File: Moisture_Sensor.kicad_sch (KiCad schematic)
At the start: 17 parts, among them J1 UPDI, J2 OLED SSD1306 0.96in, J3 STEMMA QT soil sensor, J5 BATTERY 2xAAA, Q1 DMG3415U, SW1 READ, U1 ATtiny1614-SSNR, U2 TPS22917DBVR

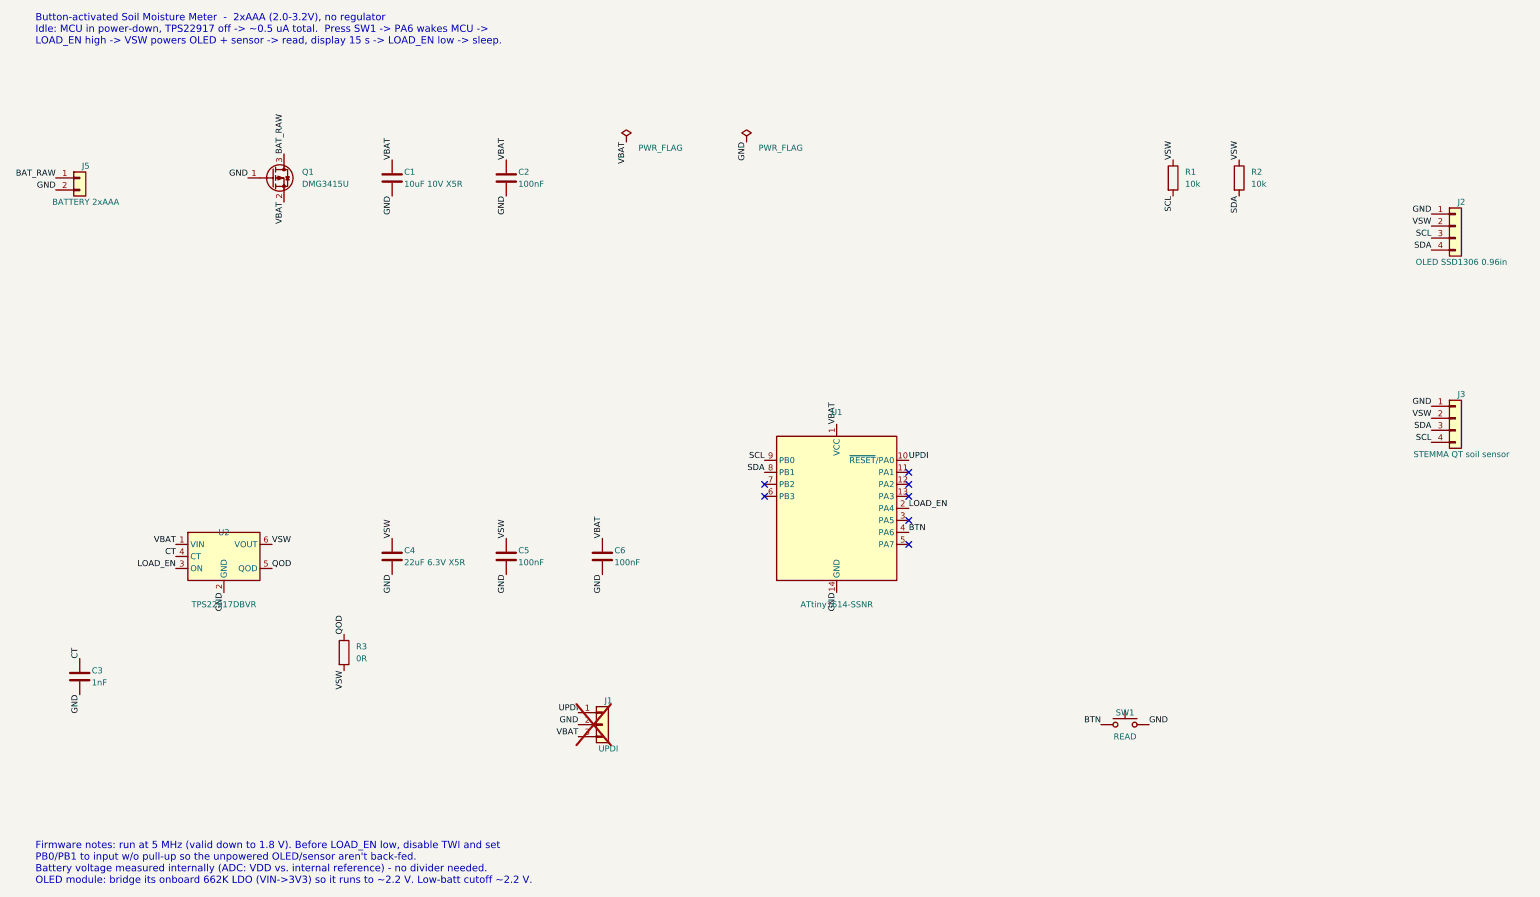
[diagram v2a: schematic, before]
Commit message: Rev C: 3xAAA, analog soil sensor, panel button, UPDI edge pads; 24x19 mm board
Co-authored-by: Copilot App <223556219+Copilot@users.noreply.github.com>
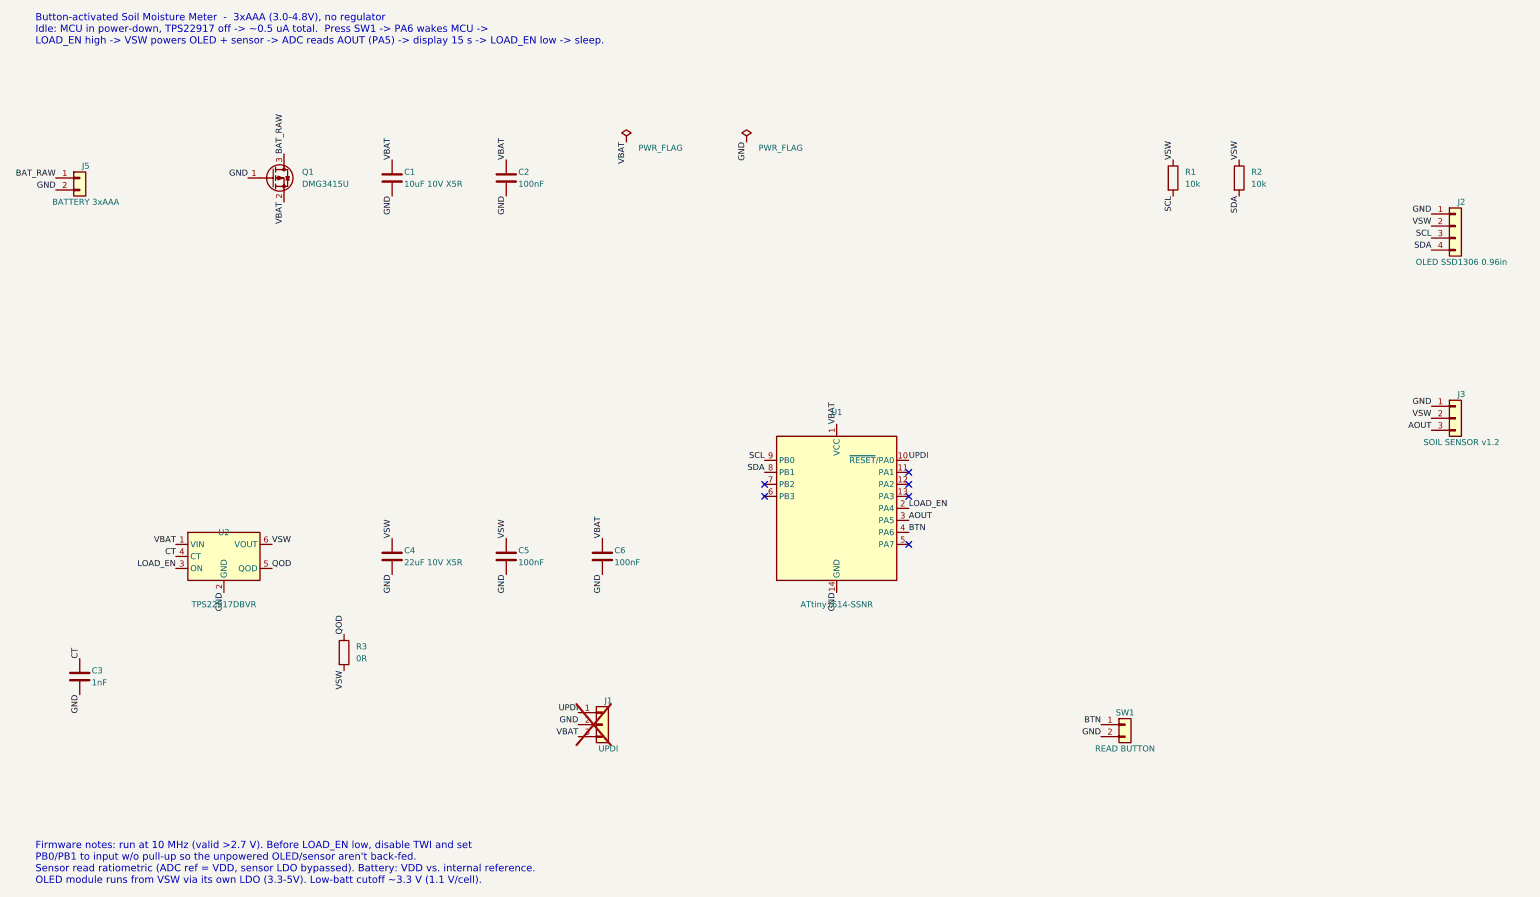
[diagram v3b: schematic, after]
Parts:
- C4: value 22uF 6.3V X5R -> 22uF 10V X5R; MPN CL21A226MQQNNNE -> CL21A226MPQNNNE
- J1: footprint Connector_PinHeader_2.54mm:PinHeader_1x03_P2.54mm_Vertical_SMD_Pin1Left -> Connector_PinHeader_2.54mm:PinHeader_1x03_P2.54mm_Vertical; Note UPDI programming pads on PCB bottom (pogo / temporary heade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 -> UPDI through-hole pads on board edge; plug Dupont wires / t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
- J3: value STEMMA QT soil sensor -> SOIL SENSOR v1.2; footprint Connector_JST:JST_SH_SM04B-SRSS-TB_1x04-1MP_P1.00mm_Horizontal -> Connector_PinHeader_2.54mm:PinHeader_1x03_P2.54mm_Vertical; symbol Connector_Generic:Conn_01x04 -> Connector_Generic:Conn_01x03; MPN SM04B-SRSS-TB(LF)(SN) -> Supplied PH2.0-3P to Dupont cable soldered to pads; Manufacturer JST -> DIYmall; Note Adafruit 4026 capacitive soil sensor (I2C 0x36) -> Capacitive soil sensor v1.2, analog 0-3V, GND-VCC-AOUT; byp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
- J5: value BATTERY 2xAAA -> BATTERY 3xAAA; Note 2xAAA holder with JST-PH leads, in case (pin1 = +) -> 3xAAA holder (3.0-4.8V) with JST-PH leads, in case (pin1 = 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
- SW1: value READ -> READ BUTTON; footprint Button_Switch_SMD:SW_Push_1P1T_NO_CK_KMR2 -> Connector_PinHeader_2.54mm:PinHeader_1x02_P2.54mm_Vertical; symbol Switch:SW_Push -> Connector_Generic:Conn_01x02; MPN KMR221GLFS -> PBS-110-XBK; Manufacturer C&K -> Twidec; Note (none) -> 7mm panel-mount momentary NO pushbutton, leads soldered to 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
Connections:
- net SCL: no longer J3.4 (Pin_4)
- net SDA: no longer J3.3 (Pin_3)
- net AOUT: now reaches U1.3 (PA5)
- net AOUT: now also J3.3 (Pin_3)
- no-connect marks 7 -> 6
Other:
- note added: "Button-activated Soil Moisture Meter - 3xAAA (3.0-4.8V), no regulator Idle: MCU in power-down, TPS22917 off -> ~0.5 uA total. Press SW1 -> PA6 wakes MCU -> LOAD_EN high -> VSW powers OLED + sensor -> ADC reads AOUT (PA5) -> display 15 s -> LOAD_EN low -> sleep."
- note added: "Firmware notes: run at 10 MHz (valid >2.7 V). Before LOAD_EN low, disable TWI and set PB0/PB1 to input w/o pull-up so the unpowered OLED/sensor aren't back-fed. Sensor read ratiometric (ADC ref = VDD, sensor LDO bypassed). Battery: VDD vs. internal reference. OLED module runs from VSW via its own LDO (3.3-5V). Low-batt cutoff ~3.3 V (1.1 V/cell)."
- note removed: "Button-activated Soil Moisture Meter - 2xAAA (2.0-3.2V), no regulator Idle: MCU in power-down, TPS22917 off -> ~0.5 uA total. Press SW1 -> PA6 wakes MCU -> LOAD_EN high -> VSW powers OLED + sensor -> read, display 15 s -> LOAD_EN low -> sleep."
- note removed: "Firmware notes: run at 5 MHz (valid down to 1.8 V). Before LOAD_EN low, disable TWI and set PB0/PB1 to input w/o pull-up so the unpowered OLED/sensor aren't back-fed. Battery voltage measured internally (ADC: VDD vs. internal reference) - no divider needed. OLED module: bridge its onboard 662K LDO (VIN->3V3) so it runs to ~2.2 V. Low-batt cutoff ~2.2 V."
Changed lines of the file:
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@@
 			)
 		)
-		(property "Value" "BATTERY 2xAAA"
+		(property "Value" "BATTERY 3xAAA"
 			(at 40.64 64.77 0)
 			(effects
@@
 			)
 		)
-		(property "Note" "2xAAA holder with JST-PH leads, in case (pin1 = +)"
+		(property "Note" "3xAAA holder (3.0-4.8V) with JST-PH leads, in case (pin1 = +)"
 			(at 39.37 59.69 0)
 			(hide yes)
@@
 		)
 	)
-	(no_connect
-		(at 214.63 132.08)
+	(label "AOUT"
+		(at 214.63 132.08 0)
+		(effects
+			(font
+				(size 1.27 1.27)
+			)
+			(justify left bottom)
+		)
 	)
 	(label "BTN"
@@
 			)
 		)
-		(property "Footprint" "Connector_PinHeader_2.54mm:PinHeader_1x03_P2.54mm_Vertical_SMD_Pin1Left"
+		(property "Footprint" "Connector_PinHeader_2.54mm:PinHeader_1x03_P2.54mm_Vertical"
 			(at 149.86 175.26 0)
 			(hide yes)
@@
 			)
 		)
-		(property "Note" "UPDI programming pads on PCB bottom (pogo / temporary header)"
+		(property "Note" "UPDI through-hole pads on board edge; plug Dupont wires / temporary header (3.3V SerialUPDI)"
 			(at 149.86 175.26 0)
 			(hide yes)
@@
 	)
 	(symbol
-		(lib_id "Switch:SW_Push")
+		(lib_id "Connector_Generic:Conn_01x02")
 		(at 260.35 175.26 0)
 		(unit 1)
@@
 			)
 		)
-		(property "Value" "READ"
-			(at 260.35 177.8 0)
-			(effects
-				(font
-					(size 1.27 1.27)
-				)
-			)
-		)
-		(property "Footprint" "Button_Switch_SMD:SW_Push_1P1T_NO_CK_KMR2"
+		(property "Value" "READ BUTTON"
+			(at 260.35 180.34 0)
+			(effects
+				(font
+					(size 1.27 1.27)
+				)
+			)
+		)
+		(property "Footprint" "Connector_PinHeader_2.54mm:PinHeader_1x02_P2.54mm_Vertical"
 			(at 260.35 175.26 0)
 			(hide yes)
@@
 			)
 		)
-		(property "MPN" "KMR221GLFS"
+		(property "MPN" "PBS-110-XBK"
 			(at 260.35 175.26 0)
 			(hide yes)
@@
 			)
 		)
-		(property "Manufacturer" "C&K"
+		(property "Manufacturer" "Twidec"
+			(at 260.35 175.26 0)
+			(hide yes)
+			(effects
+				(font
+					(size 1.27 1.27)
+				)
+			)
+		)
+		(property "Note" "7mm panel-mount momentary NO pushbutton, leads soldered to pads"
 			(at 260.35 175.26 0)
 			(hide yes)
@@
 	)
 	(label "GND"
-		(at 265.43 175.26 0)
-		(effects
-			(font
-				(size 1.27 1.27)
-			)
-			(justify left bottom)
+		(at 255.27 177.8 180)
+		(effects
+			(font
+				(size 1.27 1.27)
+			)
+			(justify right bottom)
 		)
 	)
@@
 			)
 		)
-		(property "Value" "22uF 6.3V X5R"
+		(property "Value" "22uF 10V X5R"
 			(at 107.95 140.97 0)
 			(effects
@@
 			)
 		)
-		(property "MPN" "CL21A226MQQNNNE"
+		(property "MPN" "CL21A226MPQNNNE"
 			(at 105.41 139.7 0)
 			(hide yes)
@@
 	)
 	(symbol
-		(lib_id "Connector_Generic:Conn_01x04")
+		(lib_id "Connector_Generic:Conn_01x03")
 		(at 330.2 110.49 0)
 		(unit 1)
@@
 			)
 		)
-		(property "Value" "STEMMA QT soil sensor"
-			(at 331.47 118.11 0)
-			(effects
-				(font
-					(size 1.27 1.27)
-				)
-			)
-		)
-		(property "Footprint" "Connector_JST:JST_SH_SM04B-SRSS-TB_1x04-1MP_P1.00mm_Horizontal"
+		(property "Value" "SOIL SENSOR v1.2"
+			(at 331.47 115.57 0)
+			(effects
+				(font
+					(size 1.27 1.27)
+				)
+			)
+		)
+		(property "Footprint" "Connector_PinHeader_2.54mm:PinHeader_1x03_P2.54mm_Vertical"
 			(at 330.2 110.49 0)
 			(hide yes)
@@
 			)
 		)
-		(property "MPN" "SM04B-SRSS-TB(LF)(SN)"
+		(property "MPN" "Supplied PH2.0-3P to Dupont cable soldered to pads"
 			(at 330.2 110.49 0)
 			(hide yes)
@@
 			)
 		)
-		(property "Manufacturer" "JST"
+		(property "Manufacturer" "DIYmall"
 			(at 330.2 110.49 0)
 			(hide yes)
@@
 			)
 		)
-		(property "Note" "Adafruit 4026 capacitive soil sensor (I2C 0x36)"
+		(property "Note" "Capacitive soil sensor v1.2, analog 0-3V, GND-VCC-AOUT; bypass its 662K LDO"
 			(at 330.2 110.49 0)
 			(hide yes)
@@
 		)
 		(pin "3"
-		)
-		(pin "4"
 		)
 		(instances
@@
 		)
 	)
-	(label "SDA"
+	(label "AOUT"
 		(at 325.12 113.03 180)
 		(effects
@@
 		)
 	)
-	(label "SCL"
-		(at 325.12 115.57 180)
-		(effects
-			(font
-				(size 1.27 1.27)
-			)
-			(justify right bottom)
-		)
-	)
-	(text "Button-activated Soil Moisture Meter  -  2xAAA (2.0-3.2V), no regulator\nIdle: MCU in power-down, TPS22917 off -> ~0.5 uA total.  Press SW1 -> PA6 wakes MCU ->\nLOAD_EN high -> VSW powers OLED + sensor -> read, display 15 s -> LOAD_EN low -> sleep."
+	(text "Button-activated Soil Moisture Meter  -  3xAAA (3.0-4.8V), no regulator\nIdle: MCU in power-down, TPS22917 off -> ~0.5 uA total.  Press SW1 -> PA6 wakes MCU ->\nLOAD_EN high -> VSW powers OLED + sensor -> ADC reads AOUT (PA5) -> display 15 s -> LOAD_EN low -> sleep."
 		(exclude_from_sim no)
 		(at 30 25 0)
@@
 		)
 	)
-	(text "Firmware notes: run at 5 MHz (valid down to 1.8 V). Before LOAD_EN low, disable TWI and set\nPB0/PB1 to input w/o pull-up so the unpowered OLED/sensor aren't back-fed.\nBattery voltage measured internally (ADC: VDD vs. internal reference) - no divider needed.\nOLED module: bridge its onboard 662K LDO (VIN->3V3) so it runs to ~2.2 V. Low-batt cutoff ~2.2 V."
+	(text "Firmware notes: run at 10 MHz (valid >2.7 V). Before LOAD_EN low, disable TWI and set\nPB0/PB1 to input w/o pull-up so the unpowered OLED/sensor aren't back-fed.\nSensor read ratiometric (ADC ref = VDD, sensor LDO bypassed). Battery: VDD vs. internal reference.\nOLED module runs from VSW via its own LDO (3.3-5V). Low-batt cutoff ~3.3 V (1.1 V/cell)."
 		(exclude_from_sim no)
 		(at 30 200 0)
